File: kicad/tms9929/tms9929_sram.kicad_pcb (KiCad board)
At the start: 2 copper layers, 160 x 100.3 mm, 70 parts, among them P1 CONN_01X03, P4 Power, P5 CONN_02X25, Q1 BC550, Q10 BC550, Q2 BC550, Q3 BC550, Q4 BC550, Q5 BC550, Q6 BC550, Q7 BC550, Q8 BC550, Q9 BC550, U1 TMS9929A, U10 7400, U2 74HCT04, U3 74HCT574, U4 74HCT574, U5 74HCT574, U6 HM62256BLFP-5SLT

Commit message: +final - pcb pool order
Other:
- board text added: "+12V"
- board text added: "+5V"
- board text added: "B"
- board text added: "B-Y"
- board text added: "G"
- board text added: "R"
- board text added: "R-Y"
- board text added: "Y"

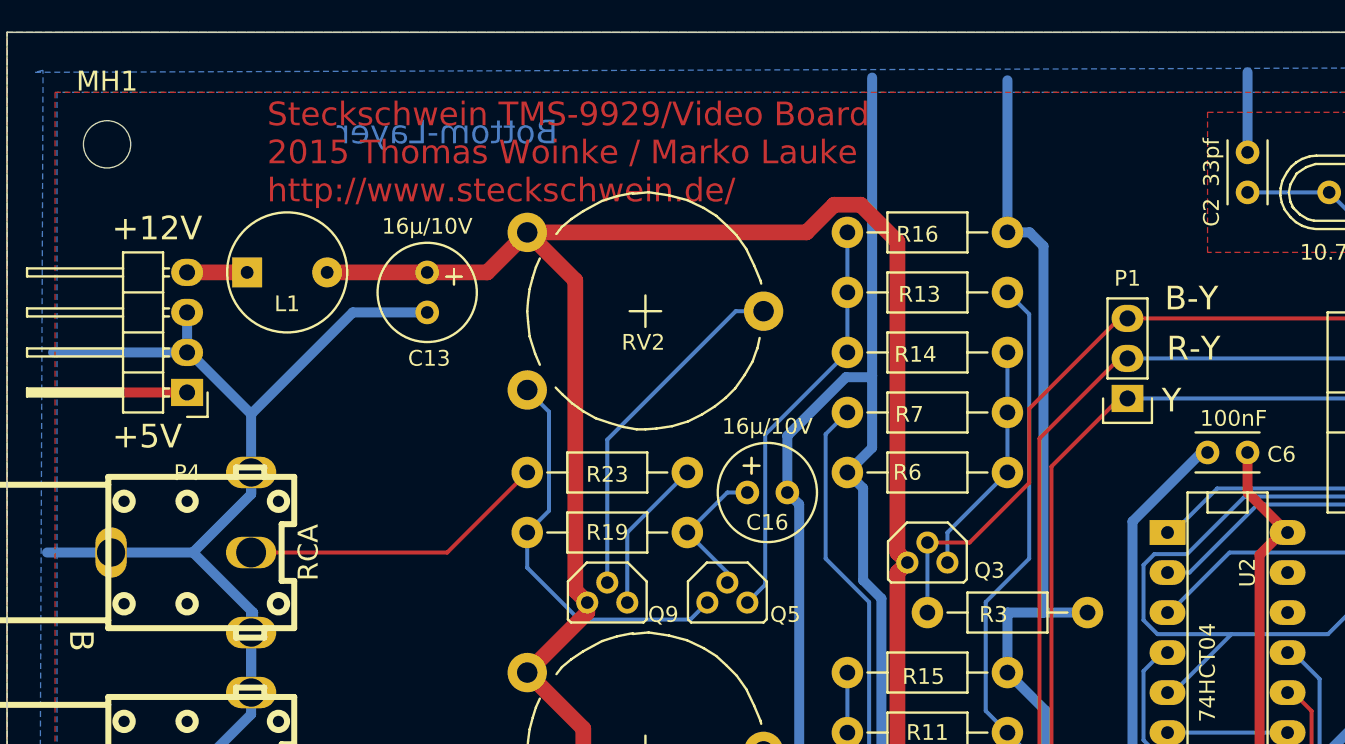
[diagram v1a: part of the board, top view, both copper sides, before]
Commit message: +fix "restringe"
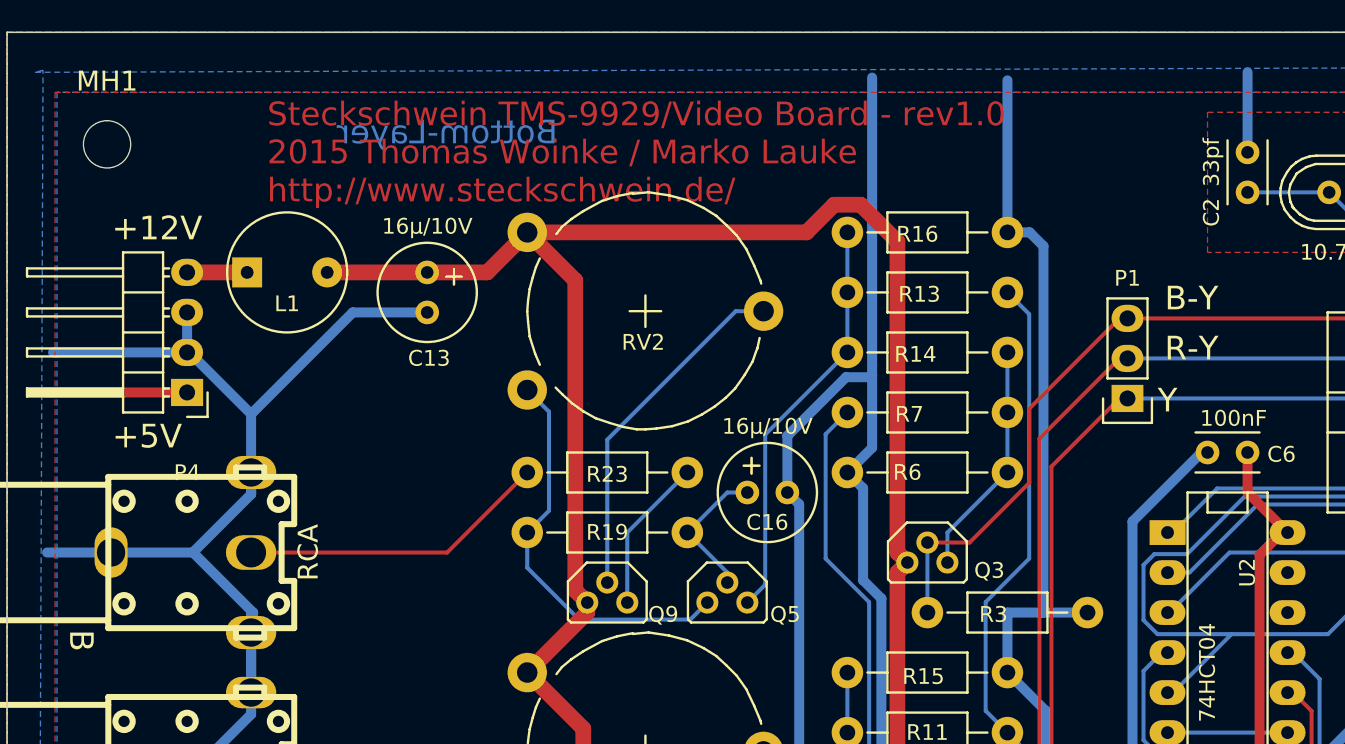
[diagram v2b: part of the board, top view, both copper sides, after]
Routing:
- net /R-Y: track 74.6 -> 73.1 mm
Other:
- board text added: "Steckschwein TMS-9929/Video Board - rev1.0 2015 Thomas Woinke / Marko Lauke http://www.steckschwein.de/"
- board text removed: "Steckschwein TMS-9929/Video Board 2015 Thomas Woinke / Marko Lauke http://www.steckschwein.de/"

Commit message: +update
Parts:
- Red1, Sync1: footprint qrcode:rca_black -> diverse:rca_black
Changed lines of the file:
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@@
     (links 226)
     (no_connects 0)
-    (area 45.516073 41.402 240.711447 146.100001)
+    (area 62.179999 45.669999 222.300001 146.100001)
     (thickness 1.6)
     (drawings 18)
@@
   )
   (module qrcode:rca_black (layer F.Cu)
-    (at 73.66 106.68 270)
+    (at 73.66 92.71 270)
     (descr "RCA Audio connector, black, Pro Signal p/n PSG01544")
     (tags "rca, audio")
-    (fp_text reference Red1 (at 0 15.7988 270) (layer F.SilkS)
+    (fp_text reference Green1 (at 0 15.7988 270) (layer F.SilkS)
       (effects (font (thickness 0.3048)))
     )
@@
       (net 1 GND))
     (pad 2 thru_hole oval (at 0 -4.064 270) (size 1.99898 3.19786) (drill 1.9) (layers *.Cu *.Mask F.SilkS)
-      (net 85 /RGB-R))
+      (net 42 /RGB-G))
     (model walter/conn_av/rca_black.wrl
       (at (xyz 0 0 0))
@@
     )
   )
-  (module qrcode:rca_black (layer F.Cu)
-    (at 73.66 120.65 270)
+  (module diverse:rca_black (layer F.Cu)
+    (at 73.66 106.68 270)
     (descr "RCA Audio connector, black, Pro Signal p/n PSG01544")
     (tags "rca, audio")
-    (fp_text reference Sync1 (at 0 15.7988 270) (layer F.SilkS)
+    (fp_text reference Red1 (at 0 15.7988 270) (layer F.SilkS)
       (effects (font (thickness 0.3048)))
     )
@@
     (fp_line (start -4.8006 4.99872) (end -4.8006 -6.80212) (layer F.SilkS) (width 0.381))
     (fp_line (start 4.8006 -6.79958) (end 4.8006 5.00126) (layer F.SilkS) (width 0.381))
-    (pad 1 thru_hole oval (at 5.08 -4.064 270) (size 1.99898 3.19786) (drill 1.8) (layers *.Cu *.Mask F.SilkS)
+    (pad 1 thru_hole oval (at 5.08 -4.064 270) (size 2.1 3.19786) (drill 1.8) (layers *.Cu *.Mask F.SilkS)
       (net 1 GND))
-    (pad 1 thru_hole oval (at 0 4.826 270) (size 3.19786 1.99898) (drill 1.8) (layers *.Cu *.Mask F.SilkS)
+    (pad 1 thru_hole oval (at 0 4.826 270) (size 3.19786 2.1) (drill 1.8) (layers *.Cu *.Mask F.SilkS)
       (net 1 GND))
-    (pad 1 thru_hole oval (at -5.08 -4.064 270) (size 1.99898 3.19786) (drill 1.8) (layers *.Cu *.Mask F.SilkS)
+    (pad 1 thru_hole oval (at -5.08 -4.064 270) (size 2.1 3.19786) (drill 1.8) (layers *.Cu *.Mask F.SilkS)
       (net 1 GND))
-    (pad 2 thru_hole oval (at 0 -4.064 270) (size 1.99898 3.19786) (drill 1.9) (layers *.Cu *.Mask F.SilkS)
-      (net 41 /SYNC))
+    (pad 2 thru_hole oval (at 0 -4.064 270) (size 2.2 3.19786) (drill 1.9) (layers *.Cu *.Mask F.SilkS)
+      (net 85 /RGB-R))
     (model walter/conn_av/rca_black.wrl
       (at (xyz 0 0 0))
@@
     )
   )
-  (module qrcode:rca_black (layer F.Cu)
-    (at 73.66 92.71 270)
+  (module diverse:rca_black (layer F.Cu)
+    (at 73.66 120.65 270)
     (descr "RCA Audio connector, black, Pro Signal p/n PSG01544")
     (tags "rca, audio")
-    (fp_text reference Green1 (at 0 15.7988 270) (layer F.SilkS)
+    (fp_text reference Sync1 (at 0 15.7988 270) (layer F.SilkS)
       (effects (font (thickness 0.3048)))
     )
@@
     (fp_line (start -4.8006 4.99872) (end -4.8006 -6.80212) (layer F.SilkS) (width 0.381))
     (fp_line (start 4.8006 -6.79958) (end 4.8006 5.00126) (layer F.SilkS) (width 0.381))
-    (pad 1 thru_hole oval (at 5.08 -4.064 270) (size 1.99898 3.19786) (drill 1.8) (layers *.Cu *.Mask F.SilkS)
+    (pad 1 thru_hole oval (at 5.08 -4.064 270) (size 2.1 3.19786) (drill 1.8) (layers *.Cu *.Mask F.SilkS)
       (net 1 GND))
-    (pad 1 thru_hole oval (at 0 4.826 270) (size 3.19786 1.99898) (drill 1.8) (layers *.Cu *.Mask F.SilkS)
+    (pad 1 thru_hole oval (at 0 4.826 270) (size 3.19786 2.1) (drill 1.8) (layers *.Cu *.Mask F.SilkS)
       (net 1 GND))
-    (pad 1 thru_hole oval (at -5.08 -4.064 270) (size 1.99898 3.19786) (drill 1.8) (layers *.Cu *.Mask F.SilkS)
+    (pad 1 thru_hole oval (at -5.08 -4.064 270) (size 2.1 3.19786) (drill 1.8) (layers *.Cu *.Mask F.SilkS)
       (net 1 GND))
-    (pad 2 thru_hole oval (at 0 -4.064 270) (size 1.99898 3.19786) (drill 1.9) (layers *.Cu *.Mask F.SilkS)
-      (net 42 /RGB-G))
+    (pad 2 thru_hole oval (at 0 -4.064 270) (size 2.2 3.19786) (drill 1.9) (layers *.Cu *.Mask F.SilkS)
+      (net 41 /SYNC))
     (model walter/conn_av/rca_black.wrl
       (at (xyz 0 0 0))

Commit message: +update rev.1.1
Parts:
- added C10: 5-50pf, Capacitors_ThroughHole:C_Disc_D6_P5, F.Cu at (162.6, 53.3)
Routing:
- net GND: track 822.8 -> 836.7 mm
- net Net-(10.738MHz1-Pad1): track 12.1 -> 19.5 mm
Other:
- board text added: "Steckschwein TMS-9929/Video Board - rev1.1 2015 Thomas Woinke / Marko Lauke http://www.steckschwein.de/"
- board text removed: "Steckschwein TMS-9929/Video Board - rev1.0 2015 Thomas Woinke / Marko Lauke http://www.steckschwein.de/"
